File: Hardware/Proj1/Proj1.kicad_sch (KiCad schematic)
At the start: 0 parts

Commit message: proj1 schematic
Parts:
- added D1: LED, symbol device:LED
- added J1: Conn_01x02, symbol Connector_Generic:Conn_01x02
- added R1: R_US, symbol Device:R_US
- added SW1: SW_Push, symbol Switch:SW_Push
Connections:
- new net: R1.1, SW1.2
- new net: D1.2 (A), R1.2
- new net +3V3: J1.1 (Pin_1), SW1.1
- new net GND: D1.1 (K), J1.2 (Pin_2)

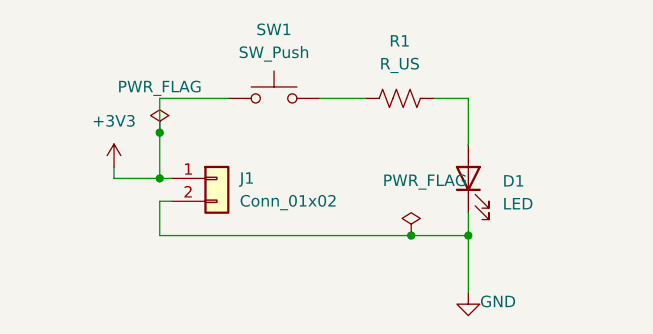
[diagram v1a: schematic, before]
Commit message: LED project schematic
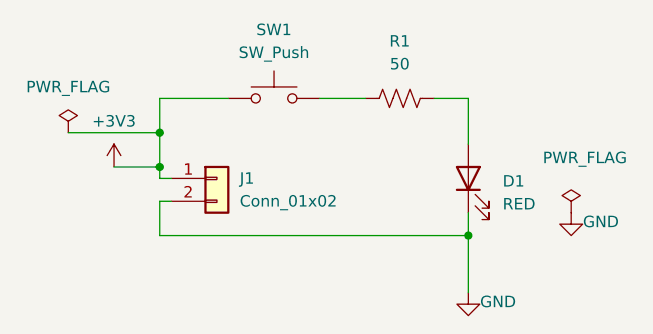
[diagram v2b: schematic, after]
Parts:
- D1: value LED -> RED; footprint (none) -> layout:LED_0603_Symbol_on_F.SilkS
- J1: footprint (none) -> Connector_Molex:Molex_KK-254_AE-6410-02A_1x02_P2.54mm_Vertical; MPN (none) -> 22-27-2021
- R1: value R_US -> 50; footprint (none) -> Resistor_SMD:R_0603_1608Metric_Pad0.98x0.95mm_HandSolder
- SW1: footprint (none) -> Button_Switch_THT:SW_PUSH_6mm; MPN (none) -> B3F-1000
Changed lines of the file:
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@@
 	)
 	(junction
-		(at 82.55 96.52)
-		(diameter 0)
-		(color 0 0 0 0)
-	)
-	(junction
-		(at 110.49 102.87)
+		(at 82.55 95.25)
 		(diameter 0)
 		(color 0 0 0 0)
@@
 	(wire
 		(pts
-			(xy 116.84 102.87) (xy 110.49 102.87)
+			(xy 82.55 95.25) (xy 82.55 96.52)
 		)
 		(stroke
@@
 	(wire
 		(pts
-			(xy 110.49 102.87) (xy 82.55 102.87)
+			(xy 72.39 91.44) (xy 82.55 91.44)
+		)
+		(stroke
+			(width 0)
+			(type default)
+		)
+	)
+	(wire
+		(pts
+			(xy 82.55 102.87) (xy 116.84 102.87)
 		)
 		(stroke
@@
 	(wire
 		(pts
-			(xy 77.47 95.25) (xy 77.47 96.52)
-		)
-		(stroke
-			(width 0)
-			(type default)
-		)
-	)
-	(wire
-		(pts
 			(xy 82.55 99.06) (xy 82.55 102.87)
 		)
@@
 	(wire
 		(pts
+			(xy 77.47 95.25) (xy 82.55 95.25)
+		)
+		(stroke
+			(width 0)
+			(type default)
+		)
+	)
+	(wire
+		(pts
 			(xy 100.33 87.63) (xy 105.41 87.63)
 		)
@@
 	(wire
 		(pts
-			(xy 82.55 91.44) (xy 82.55 96.52)
-		)
-		(stroke
-			(width 0)
-			(type default)
-		)
-	)
-	(wire
-		(pts
-			(xy 82.55 96.52) (xy 77.47 96.52)
+			(xy 82.55 91.44) (xy 82.55 95.25)
 		)
 		(stroke
@@
 			)
 		)
-		(property "Value" "R_US"
+		(property "Value" "50"
 			(at 109.22 83.82 90)
 			(effects
@@
 			)
 		)
-		(property "Footprint" ""
+		(property "Footprint" "Resistor_SMD:R_0603_1608Metric_Pad0.98x0.95mm_HandSolder"
 			(at 109.474 86.614 90)
 			(effects
@@
 		(property "Description" "Resistor, US symbol"
 			(at 109.22 87.63 0)
+			(effects
+				(font
+					(size 1.27 1.27)
+				)
+				(hide yes)
+			)
+		)
+		(property "MPN" ""
+			(at 109.22 87.63 90)
 			(effects
 				(font
@@
 	(symbol
 		(lib_id "power:PWR_FLAG")
-		(at 82.55 91.44 0)
+		(at 72.39 91.44 0)
 		(unit 1)
 		(exclude_from_sim no)
@@
 		(fields_autoplaced yes)
 		(property "Reference" "#FLG02"
-			(at 82.55 89.535 0)
+			(at 72.39 89.535 0)
 			(effects
 				(font
@@
 		)
 		(property "Value" "PWR_FLAG"
-			(at 82.55 86.36 0)
+			(at 72.39 86.36 0)
 			(effects
 				(font
@@
 		)
 		(property "Footprint" ""
-			(at 82.55 91.44 0)
+			(at 72.39 91.44 0)
 			(effects
 				(font
@@
 		)
 		(property "Datasheet" "~"
-			(at 82.55 91.44 0)
+			(at 72.39 91.44 0)
 			(effects
 				(font
@@
 		)
 		(property "Description" "Special symbol for telling ERC where power comes from"
-			(at 82.55 91.44 0)
+			(at 72.39 91.44 0)
 			(effects
 				(font
@@
 			)
 		)
-		(property "Footprint" ""
+		(property "Footprint" "Button_Switch_THT:SW_PUSH_6mm"
 			(at 95.25 82.55 0)
 			(effects
@@
 			)
 		)
-		(property "Datasheet" "~"
+		(property "Datasheet" "https://www.omron.com/ecb/products/pdf/en-b3f.pdf"
 			(at 95.25 82.55 0)
 			(effects
@@
 		)
 		(property "Description" "Push button switch, generic, two pins"
+			(at 95.25 87.63 0)
+			(effects
+				(font
+					(size 1.27 1.27)
+				)
+				(hide yes)
+			)
+		)
+		(property "MPN" "B3F-1000"
 			(at 95.25 87.63 0)
 			(effects
@@
 	(symbol
 		(lib_id "power:PWR_FLAG")
-		(at 110.49 102.87 0)
+		(at 128.27 100.33 0)
 		(unit 1)
 		(exclude_from_sim no)
@@
 		(dnp no)
 		(property "Reference" "#FLG01"
-			(at 110.49 100.965 0)
+			(at 128.27 98.425 0)
 			(effects
 				(font
@@
 		)
 		(property "Value" "PWR_FLAG"
-			(at 112.014 96.774 0)
+			(at 129.794 94.234 0)
 			(effects
 				(font
@@
 		)
 		(property "Footprint" ""
-			(at 110.49 102.87 0)
+			(at 128.27 100.33 0)
 			(effects
 				(font
@@
 		)
 		(property "Datasheet" "~"
-			(at 110.49 102.87 0)
+			(at 128.27 100.33 0)
 			(effects
 				(font
@@
 		)
 		(property "Description" "Special symbol for telling ERC where power comes from"
-			(at 110.49 102.87 0)
+			(at 128.27 100.33 0)
 			(effects
 				(font
@@
 	)
 	(symbol
+		(lib_id "power:GND")
+		(at 128.27 100.33 0)
+		(unit 1)
+		(exclude_from_sim no)
+		(in_bom yes)
+		(on_board yes)
+		(dnp no)
+		(property "Reference" "#PWR03"
+			(at 128.27 106.68 0)
+			(effects
+				(font
+					(size 1.27 1.27)
+				)
+				(hide yes)
+			)
+		)
+		(property "Value" "GND"
+			(at 131.572 101.346 0)
+			(effects
+				(font
+					(size 1.27 1.27)
+				)
+			)
+		)
+		(property "Footprint" ""
+			(at 128.27 100.33 0)
+			(effects
+				(font
+					(size 1.27 1.27)
+				)
+				(hide yes)
+			)
+		)
+		(property "Datasheet" ""
+			(at 128.27 100.33 0)
+			(effects
+				(font
+					(size 1.27 1.27)
+				)
+				(hide yes)
+			)
+		)
+		(property "Description" "Power symbol creates a global label with name \"GND\" , ground"
+			(at 128.27 100.33 0)
+			(effects
+				(font
+					(size 1.27 1.27)
+				)
+				(hide yes)
+			)
+		)
+		(pin "1"
+		)
+		(instances
+			(project "Proj1"
+				(path "/1e1b062d-fad0-427c-a622-c5b8a80b5268"
+					(reference "#PWR03")
+					(unit 1)
+				)
+			)
+		)
+	)
+	(symbol
 		(lib_id "device:LED")
 		(at 116.84 96.52 90)
@@
 			)
 		)
-		(property "Value" "LED"
+		(property "Value" "RED"
 			(at 120.65 99.3774 90)
 			(effects
@@
 			)
 		)
-		(property "Footprint" ""
+		(property "Footprint" "layout:LED_0603_Symbol_on_F.SilkS"
 			(at 116.84 96.52 0)
 			(effects
@@
 		(property "Description" "Light emitting diode"
 			(at 116.84 96.52 0)
+			(effects
+				(font
+					(size 1.27 1.27)
+				)
+				(hide yes)
+			)
+		)
+		(property "MPN" ""
+			(at 116.84 96.52 90)
 			(effects
 				(font
@@
 			)
 		)
-		(property "Footprint" ""
+		(property "Footprint" "Connector_Molex:Molex_KK-254_AE-6410-02A_1x02_P2.54mm_Vertical"
 			(at 88.9 96.52 0)
 			(effects
@@
 			)
 		)
-		(property "Datasheet" "~"
+		(property "Datasheet" "http://www.molex.com/pdm_docs/sd/022272021_sd.pdf"
 			(at 88.9 96.52 0)
 			(effects
@@
 			(at 88.9 96.52 0)
 			(effects
+				(font
+					(size 1.27 1.27)
+				)
+				(hide yes)
+			)
+		)
+		(property "MPN" "22-27-2021"
+			(at 88.9 96.52 0)
+			(effects

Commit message: LED project schematic final
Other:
- title: Template -> Project 1
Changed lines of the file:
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@@
 	(paper "USLetter")
 	(title_block
-		(title "Template")
-		(date "2022-08-16")
+		(title "Project 1")
+		(date "2026-09-24")
 		(rev "0.0")
 		(company "Illini Solar Car")
-		(comment 1 "Designed By: Your Name")
+		(comment 1 "Designed By: Yunpeng Tan")
 	)
 	(junction

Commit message: LED project schematic final
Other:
- title: Project 1 -> LED Project
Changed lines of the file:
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@@
 	(paper "USLetter")
 	(title_block
-		(title "Project 1")
+		(title "LED Project")
 		(date "2026-09-24")
-		(rev "0.0")
+		(rev "1.0")
 		(company "Illini Solar Car")
 		(comment 1 "Designed By: Yunpeng Tan")

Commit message: LED project schematic final
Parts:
- D1: value RED -> Red
- R1: value 50 -> 105
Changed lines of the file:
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@@
 			)
 		)
-		(property "Value" "50"
+		(property "Value" "105"
 			(at 109.22 83.82 90)
 			(effects
@@
 			)
 		)
-		(property "Value" "RED"
+		(property "Value" "Red"
 			(at 120.65 99.3774 90)
 			(effects

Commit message: Fixed Hardware easy LED project
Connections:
- net +3V3: now also J1.2 (Pin_2); no longer J1.1 (Pin_1)
- net GND: now also J1.1 (Pin_1); no longer J1.2 (Pin_2)
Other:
- moved on the sheet: J1
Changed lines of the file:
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@@
 	)
 	(junction
-		(at 116.84 102.87)
+		(at 82.55 105.41)
 		(diameter 0)
 		(color 0 0 0 0)
 	)
 	(junction
-		(at 82.55 95.25)
+		(at 82.55 90.17)
 		(diameter 0)
 		(color 0 0 0 0)
 	)
 	(junction
-		(at 82.55 91.44)
+		(at 82.55 87.63)
 		(diameter 0)
 		(color 0 0 0 0)
 	)
+	(junction
+		(at 82.55 102.87)
+		(diameter 0)
+		(color 0 0 0 0)
+	)
 	(wire
 		(pts
@@
 	(wire
 		(pts
-			(xy 82.55 95.25) (xy 82.55 96.52)
+			(xy 82.55 85.09) (xy 82.55 87.63)
 		)
 		(stroke
@@
 	(wire
 		(pts
-			(xy 83.82 96.52) (xy 82.55 96.52)
-		)
-		(stroke
-			(width 0)
-			(type default)
-		)
-	)
-	(wire
-		(pts
-			(xy 72.39 91.44) (xy 82.55 91.44)
-		)
-		(stroke
-			(width 0)
-			(type default)
-		)
-	)
-	(wire
-		(pts
 			(xy 82.55 102.87) (xy 116.84 102.87)
 		)
@@
 	(wire
 		(pts
-			(xy 82.55 87.63) (xy 82.55 91.44)
-		)
-		(stroke
-			(width 0)
-			(type default)
-		)
-	)
-	(wire
-		(pts
-			(xy 83.82 99.06) (xy 82.55 99.06)
-		)
-		(stroke
-			(width 0)
-			(type default)
-		)
-	)
-	(wire
-		(pts
-			(xy 116.84 102.87) (xy 116.84 109.22)
+			(xy 82.55 90.17) (xy 82.55 96.52)
 		)
 		(stroke
@@
 	(wire
 		(pts
-			(xy 77.47 95.25) (xy 82.55 95.25)
+			(xy 82.55 102.87) (xy 82.55 105.41)
 		)
 		(stroke
@@
 	(wire
 		(pts
-			(xy 82.55 91.44) (xy 82.55 95.25)
+			(xy 81.28 96.52) (xy 82.55 96.52)
+		)
+		(stroke
+			(width 0)
+			(type default)
+		)
+	)
+	(wire
+		(pts
+			(xy 82.55 87.63) (xy 82.55 90.17)
+		)
+		(stroke
+			(width 0)
+			(type default)
+		)
+	)
+	(wire
+		(pts
+			(xy 82.55 105.41) (xy 82.55 107.95)
+		)
+		(stroke
+			(width 0)
+			(type default)
+		)
+	)
+	(wire
+		(pts
+			(xy 81.28 99.06) (xy 82.55 99.06)
 		)
 		(stroke
@@
 	(symbol
 		(lib_id "power:PWR_FLAG")
-		(at 72.39 91.44 0)
-		(unit 1)
-		(exclude_from_sim no)
-		(in_bom yes)
-		(on_board yes)
-		(dnp no)
-		(fields_autoplaced yes)
+		(at 82.55 90.17 90)
+		(unit 1)
+		(exclude_from_sim no)
+		(in_bom yes)
+		(on_board yes)
+		(dnp no)
 		(property "Reference" "#FLG02"
-			(at 72.39 89.535 0)
+			(at 80.645 90.17 0)
 			(effects
 				(font
@@
 		)
 		(property "Value" "PWR_FLAG"
-			(at 72.39 86.36 0)
-			(effects
-				(font
-					(size 1.27 1.27)
-				)
+			(at 79.502 87.63 90)
+			(effects
+				(font
+					(size 1.27 1.27)
+				)
+				(justify left)
 			)
 		)
 		(property "Footprint" ""
-			(at 72.39 91.44 0)
+			(at 82.55 90.17 0)
 			(effects
 				(font
@@
 		)
 		(property "Datasheet" "~"
-			(at 72.39 91.44 0)
+			(at 82.55 90.17 0)
 			(effects
 				(font
@@
 		)
 		(property "Description" "Special symbol for telling ERC where power comes from"
-			(at 72.39 91.44 0)
+			(at 82.55 90.17 0)
 			(effects
 				(font
@@
 	(symbol
 		(lib_id "power:+3V3")
-		(at 77.47 95.25 0)
+		(at 82.55 85.09 0)
 		(unit 1)
 		(exclude_from_sim no)
@@
 		(fields_autoplaced yes)
 		(property "Reference" "#PWR01"
-			(at 77.47 99.06 0)
+			(at 82.55 88.9 0)
 			(effects
 				(font
@@
 		)
 		(property "Value" "+3V3"
-			(at 77.47 90.17 0)
+			(at 82.55 80.01 0)
 			(effects
 				(font
@@
 		)
 		(property "Footprint" ""
-			(at 77.47 95.25 0)
+			(at 82.55 85.09 0)
 			(effects
 				(font
@@
 		)
 		(property "Datasheet" ""
-			(at 77.47 95.25 0)
+			(at 82.55 85.09 0)
 			(effects
 				(font
@@
 		)
 		(property "Description" "Power symbol creates a global label with name \"+3V3\""
-			(at 77.47 95.25 0)
+			(at 82.55 85.09 0)
 			(effects
 				(font
@@
 	(symbol
 		(lib_id "power:GND")
-		(at 116.84 109.22 0)
+		(at 82.55 107.95 0)
 		(unit 1)
 		(exclude_from_sim no)
@@
 		(dnp no)
 		(property "Reference" "#PWR02"
-			(at 116.84 115.57 0)
+			(at 82.55 114.3 0)
 			(effects
 				(font
@@
 		)
 		(property "Value" "GND"
-			(at 120.142 110.236 0)
+			(at 85.852 108.966 0)
 			(effects
 				(font
@@
 		)
 		(property "Footprint" ""
-			(at 116.84 109.22 0)
+			(at 82.55 107.95 0)
 			(effects
 				(font
@@
 		)
 		(property "Datasheet" ""
-			(at 116.84 109.22 0)
+			(at 82.55 107.95 0)
 			(effects
 				(font
@@
 		)
 		(property "Description" "Power symbol creates a global label with name \"GND\" , ground"
-			(at 116.84 109.22 0)
+			(at 82.55 107.95 0)
 			(effects
 				(font
@@
 	(symbol
 		(lib_id "power:PWR_FLAG")
-		(at 128.27 100.33 0)
+		(at 82.55 105.41 90)
 		(unit 1)
 		(exclude_from_sim no)
@@
 		(dnp no)
 		(property "Reference" "#FLG01"
-			(at 128.27 98.425 0)
+			(at 80.645 105.41 0)
 			(effects
 				(font
@@
 		)
 		(property "Value" "PWR_FLAG"
-			(at 129.794 94.234 0)
+			(at 74.168 105.41 90)
 			(effects
 				(font
@@
 		)
 		(property "Footprint" ""
-			(at 128.27 100.33 0)
+			(at 82.55 105.41 0)
 			(effects
 				(font
@@
 		)
 		(property "Datasheet" "~"
-			(at 128.27 100.33 0)
+			(at 82.55 105.41 0)
 			(effects
 				(font
@@
 		)
 		(property "Description" "Special symbol for telling ERC where power comes from"
-			(at 128.27 100.33 0)
+			(at 82.55 105.41 0)
 			(effects
 				(font
@@
 	)
 	(symbol
-		(lib_id "power:GND")
-		(at 128.27 100.33 0)
-		(unit 1)
-		(exclude_from_sim no)
-		(in_bom yes)
-		(on_board yes)
-		(dnp no)
-		(property "Reference" "#PWR03"
-			(at 128.27 106.68 0)
-			(effects
-				(font
-					(size 1.27 1.27)
-				)
-				(hide yes)
-			)
-		)
-		(property "Value" "GND"
-			(at 131.572 101.346 0)
-			(effects
-				(font
-					(size 1.27 1.27)
-				)
-			)
-		)
-		(property "Footprint" ""
-			(at 128.27 100.33 0)
-			(effects
-				(font
-					(size 1.27 1.27)
-				)
-				(hide yes)
-			)
-		)
-		(property "Datasheet" ""
-			(at 128.27 100.33 0)
-			(effects
-				(font
-					(size 1.27 1.27)
-				)
-				(hide yes)
-			)
-		)
-		(property "Description" "Power symbol creates a global label with name \"GND\" , ground"
-			(at 128.27 100.33 0)
-			(effects
-				(font
-					(size 1.27 1.27)
-				)
-				(hide yes)
-			)
-		)
-		(pin "1"
-		)
-		(instances
-			(project "Proj1"
-				(path "/1e1b062d-fad0-427c-a622-c5b8a80b5268"
-					(reference "#PWR03")
-					(unit 1)
-				)
-			)
-		)
-	)
-	(symbol
 		(lib_id "device:LED")
 		(at 116.84 96.52 90)
@@
 	(symbol
 		(lib_id "Connector_Generic:Conn_01x02")
-		(at 88.9 96.52 0)
+		(at 76.2 99.06 180)
 		(unit 1)
 		(exclude_from_sim no)
@@
 		(fields_autoplaced yes)
 		(property "Reference" "J1"
-			(at 91.44 96.5199 0)
-			(effects
-				(font
-					(size 1.27 1.27)
-				)
-				(justify left)
+			(at 76.2 90.17 0)
+			(effects
+				(font
+					(size 1.27 1.27)
+				)
 			)
 		)
 		(property "Value" "Conn_01x02"
-			(at 91.44 99.0599 0)
-			(effects
-				(font
-					(size 1.27 1.27)
-				)
-				(justify left)
+			(at 76.2 92.71 0)
+			(effects
+				(font
+					(size 1.27 1.27)
+				)
 			)
 		)
 		(property "Footprint" "Connector_Molex:Molex_KK-254_AE-6410-02A_1x02_P2.54mm_Vertical"
-			(at 88.9 96.52 0)
+			(at 76.2 99.06 0)
 			(effects
 				(font
@@
 		)
 		(property "Datasheet" "http://www.molex.com/pdm_docs/sd/022272021_sd.pdf"
-			(at 88.9 96.52 0)
+			(at 76.2 99.06 0)
 			(effects
 				(font
@@
 		)
 		(property "Description" "Generic connector, single row, 01x02, script generated (kicad-library-utils/schlib/autogen/connector/)"
-			(at 88.9 96.52 0)
+			(at 76.2 99.06 0)
 			(effects
 				(font
@@
 		)
 		(property "MPN" "22-27-2021"
-			(at 88.9 96.52 0)
-			(effects
-				(font
+			(at 76.2 99.06 0)
+			(effects
+				(font
